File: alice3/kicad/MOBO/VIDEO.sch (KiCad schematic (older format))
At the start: 15 parts, among them SW1 RESET, U1 Propeller_P8X32A-D40, U2 VGA_daughter_board, U3 24LC256, U4 Propeller_Plug, U5 LM2937-3.3, Y1 5 MHz

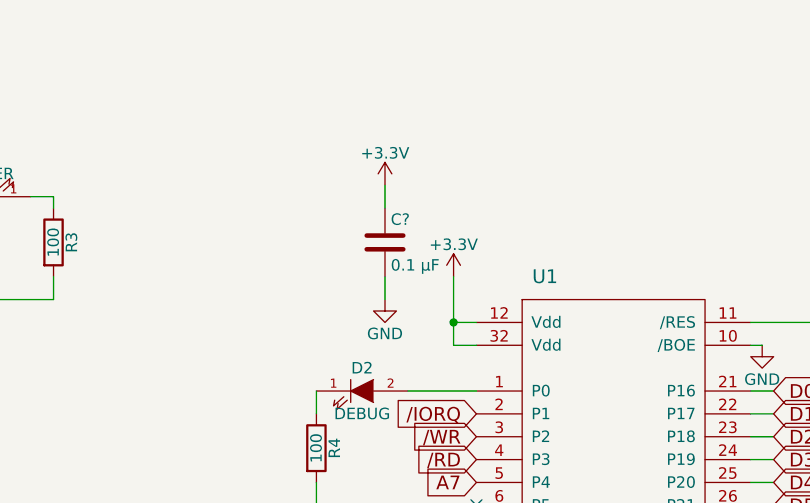
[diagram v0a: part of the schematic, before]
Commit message: Add SRAM and EEPROM.
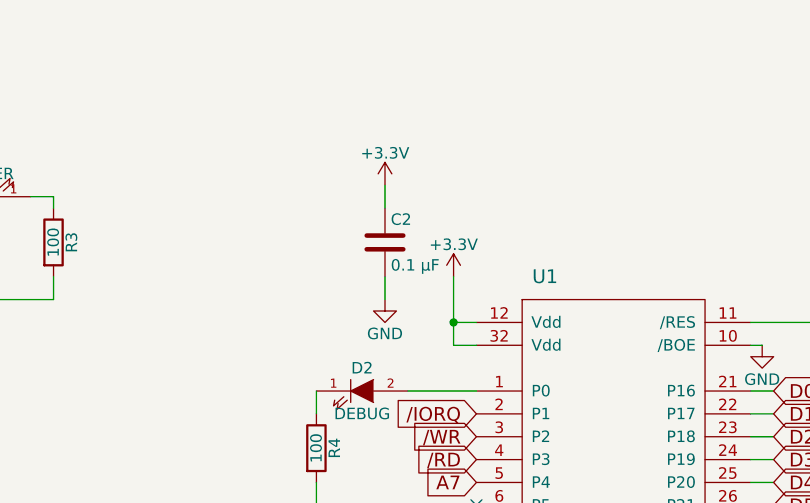
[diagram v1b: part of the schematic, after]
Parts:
- gave numbers to parts that had none: 1
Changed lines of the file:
@@
 LIBS:vga_daughter_board
 LIBS:Zilog
+LIBS:km681000blp-7
+LIBS:28f512
 LIBS:MOBO-cache
 EELAYER 25 0
@@
 $EndComp
 $Comp
-L GND #PWR01
+L GND #PWR12
 U 1 1 566E4A0D
 P 6100 4700
-F 0 "#PWR01" H 6100 4450 50  0001 C CNN
+F 0 "#PWR12" H 6100 4450 50  0001 C CNN
 F 1 "GND" H 6100 4550 50  0000 C CNN
 F 2 "" H 6100 4700 50  0000 C CNN
@@
 $EndComp
 $Comp
-L +3.3V #PWR02
+L +3.3V #PWR11
 U 1 1 566E4A37
 P 6100 2100
-F 0 "#PWR02" H 6100 1950 50  0001 C CNN
+F 0 "#PWR11" H 6100 1950 50  0001 C CNN
 F 1 "+3.3V" H 6100 2240 50  0000 C CNN
 F 2 "" H 6100 2100 50  0000 C CNN
@@
 $EndComp
 $Comp
-L +3.3V #PWR03
+L +3.3V #PWR14
 U 1 1 566E4B67
 P 7900 1700
-F 0 "#PWR03" H 7900 1550 50  0001 C CNN
+F 0 "#PWR14" H 7900 1550 50  0001 C CNN
 F 1 "+3.3V" H 7900 1840 50  0000 C CNN
 F 2 "" H 7900 1700 50  0000 C CNN
@@
 $EndComp
 $Comp
-L GND #PWR04
+L GND #PWR17
 U 1 1 566E4C07
 P 8650 2400
-F 0 "#PWR04" H 8650 2150 50  0001 C CNN
+F 0 "#PWR17" H 8650 2150 50  0001 C CNN
 F 1 "GND" H 8650 2250 50  0000 C CNN
 F 2 "" H 8650 2400 50  0000 C CNN
@@
 $EndComp
 $Comp
-L PWR_FLAG #FLG05
+L PWR_FLAG #FLG1
 U 1 1 566E4C94
 P 1000 1200
-F 0 "#FLG05" H 1000 1295 50  0001 C CNN
+F 0 "#FLG1" H 1000 1295 50  0001 C CNN
 F 1 "PWR_FLAG" H 1000 1380 50  0000 C CNN
 F 2 "" H 1000 1200 50  0000 C CNN
@@
 $EndComp
 $Comp
-L PWR_FLAG #FLG06
+L PWR_FLAG #FLG2
 U 1 1 566E4CCE
 P 1500 1200
-F 0 "#FLG06" H 1500 1295 50  0001 C CNN
+F 0 "#FLG2" H 1500 1295 50  0001 C CNN
 F 1 "PWR_FLAG" H 1500 1380 50  0000 C CNN
 F 2 "" H 1500 1200 50  0000 C CNN
@@
 $EndComp
 $Comp
-L GND #PWR07
+L GND #PWR2
 U 1 1 566E4D40
 P 1500 1500
-F 0 "#PWR07" H 1500 1250 50  0001 C CNN
+F 0 "#PWR2" H 1500 1250 50  0001 C CNN
 F 1 "GND" H 1500 1350 50  0000 C CNN
 F 2 "" H 1500 1500 50  0000 C CNN
@@
 $EndComp
 $Comp
-L GND #PWR08
+L GND #PWR16
 U 1 1 5681F164
 P 8350 4400
-F 0 "#PWR08" H 8350 4150 50  0001 C CNN
+F 0 "#PWR16" H 8350 4150 50  0001 C CNN
 F 1 "GND" H 8350 4250 50  0000 C CNN
 F 2 "" H 8350 4400 50  0000 C CNN
@@
 $EndComp
 $Comp
-L +3.3V #PWR09
+L +3.3V #PWR18
 U 1 1 5681F2C2
 P 9450 3850
-F 0 "#PWR09" H 9450 3700 50  0001 C CNN
+F 0 "#PWR18" H 9450 3700 50  0001 C CNN
 F 1 "+3.3V" H 9450 3990 50  0000 C CNN
 F 2 "" H 9450 3850 50  0000 C CNN
@@
 $EndComp
 $Comp
-L GND #PWR010
+L GND #PWR19
 U 1 1 5681F2E8
 P 9700 4150
-F 0 "#PWR010" H 9700 3900 50  0001 C CNN
+F 0 "#PWR19" H 9700 3900 50  0001 C CNN
 F 1 "GND" H 9700 4000 50  0000 C CNN
 F 2 "" H 9700 4150 50  0000 C CNN
@@
 $EndComp
 $Comp
-L +3.3V #PWR011
+L +3.3V #PWR15
 U 1 1 5681F435
 P 8100 3600
-F 0 "#PWR011" H 8100 3450 50  0001 C CNN
+F 0 "#PWR15" H 8100 3450 50  0001 C CNN
 F 1 "+3.3V" H 8100 3740 50  0000 C CNN
 F 2 "" H 8100 3600 50  0000 C CNN
@@
 $EndComp
 $Comp
-L GND #PWR012
+L GND #PWR4
 U 1 1 5681F91B
 P 2950 2350
-F 0 "#PWR012" H 2950 2100 50  0001 C CNN
+F 0 "#PWR4" H 2950 2100 50  0001 C CNN
 F 1 "GND" H 2950 2200 50  0000 C CNN
 F 2 "" H 2950 2350 50  0000 C CNN
@@
 $EndComp
 $Comp
-L +5V #PWR013
+L +5V #PWR3
 U 1 1 5681FA03
 P 2350 1650
-F 0 "#PWR013" H 2350 1500 50  0001 C CNN
+F 0 "#PWR3" H 2350 1500 50  0001 C CNN
 F 1 "+5V" H 2350 1790 50  0000 C CNN
 F 2 "" H 2350 1650 50  0000 C CNN
@@
 $EndComp
 $Comp
-L +3.3V #PWR014
+L +3.3V #PWR5
 U 1 1 5681FA32
 P 3550 1650
-F 0 "#PWR014" H 3550 1500 50  0001 C CNN
+F 0 "#PWR5" H 3550 1500 50  0001 C CNN
 F 1 "+3.3V" H 3550 1790 50  0000 C CNN
 F 2 "" H 3550 1650 50  0000 C CNN
@@
 $EndComp
 $Comp
-L +5V #PWR015
+L +5V #PWR1
 U 1 1 5681FAF3
 P 1000 1500
-F 0 "#PWR015" H 1000 1350 50  0001 C CNN
+F 0 "#PWR1" H 1000 1350 50  0001 C CNN
 F 1 "+5V" H 1000 1640 50  0000 C CNN
 F 2 "" H 1000 1500 50  0000 C CNN
@@
 $EndComp
 $Comp
-L GND #PWR016
+L GND #PWR6
 U 1 1 56821F3F
 P 5500 3100
-F 0 "#PWR016" H 5500 2850 50  0001 C CNN
+F 0 "#PWR6" H 5500 2850 50  0001 C CNN
 F 1 "GND" H 5500 2950 50  0000 C CNN
 F 2 "" H 5500 3100 50  0000 C CNN
@@
 NoConn ~ 7400 3800
 $Comp
-L GND #PWR021
+L GND #PWR13
 U 1 1 56826035
 P 7450 2400
-F 0 "#PWR021" H 7450 2150 50  0001 C CNN
+F 0 "#PWR13" H 7450 2150 50  0001 C CNN
 F 1 "GND" H 7450 2250 50  0000 C CNN
 F 2 "" H 7450 2400 50  0000 C CNN
@@
 	8300 2500 7850 2500
 $Comp
-L GND #PWR?
+L GND #PWR7
 U 1 1 568DCD28
 P 5600 4800
-F 0 "#PWR?" H 5600 4550 50  0001 C CNN
+F 0 "#PWR7" H 5600 4550 50  0001 C CNN
 F 1 "GND" H 5600 4650 50  0000 C CNN
 F 2 "" H 5600 4800 50  0000 C CNN
@@
 	5500 4800 5600 4800
 $Comp
-L +5V #PWR?
+L +5V #PWR10
 U 1 1 568DCDF3
 P 5900 4850
-F 0 "#PWR?" H 5900 4700 50  0001 C CNN
+F 0 "#PWR10" H 5900 4700 50  0001 C CNN
 F 1 "+5V" H 5900 4990 50  0000 C CNN
 F 2 "" H 5900 4850 50  0000 C CNN
@@
 /RD
 $Comp
-L C C?
+L C C2
 U 1 1 568DD525
 P 5800 1950
-F 0 "C?" H 5825 2050 50  0000 L CNN
+F 0 "C2" H 5825 2050 50  0000 L CNN
 F 1 "0.1 µF" H 5825 1850 50  0000 L CNN
 F 2 "" H 5838 1800 50  0000 C CNN
@@
 $EndComp
 $Comp
-L GND #PWR?
+L GND #PWR9
 U 1 1 568DD571
 P 5800 2200
-F 0 "#PWR?" H 5800 1950 50  0001 C CNN
+F 0 "#PWR9" H 5800 1950 50  0001 C CNN
 F 1 "GND" H 5800 2050 50  0000 C CNN
 F 2 "" H 5800 2200 50  0000 C CNN
@@
 $EndComp
 $Comp
-L +3.3V #PWR?
+L +3.3V #PWR8
 U 1 1 568DD5A9
 P 5800 1700
-F 0 "#PWR?" H 5800 1550 50  0001 C CNN
+F 0 "#PWR8" H 5800 1550 50  0001 C CNN
 F 1 "+3.3V" H 5800 1840 50  0000 C CNN
 F 2 "" H 5800 1700 50  0000 C CNN

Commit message: first draft completed integration
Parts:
- renumbered R3 to R1, R4 to R2, R1 to R3, R2 to R4, U5 to U1, U1 to U3, U3 to U4, U4 to U5
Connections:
- net CLK: now reaches U3.6 (P5)
- no-connect marks 9 -> 8
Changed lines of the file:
@@
 $EndDescr
 $Comp
-L Propeller_P8X32A-D40 U1
+L Propeller_P8X32A-D40 U3
 U 1 1 566E498F
 P 6800 3400
-F 0 "U1" H 6500 4700 60  0000 C CNN
+F 0 "U3" H 6500 4700 60  0000 C CNN
 F 1 "Propeller_P8X32A-D40" H 6800 2100 60  0000 C CNN
 F 2 "Housings_DIP:DIP-40_W25.4mm" H 6800 3200 60  0001 C CNN
@@
 $EndComp
 $Comp
-L GND #PWR12
+L GND #PWR01
 U 1 1 566E4A0D
 P 6100 4700
-F 0 "#PWR12" H 6100 4450 50  0001 C CNN
+F 0 "#PWR01" H 6100 4450 50  0001 C CNN
 F 1 "GND" H 6100 4550 50  0000 C CNN
 F 2 "" H 6100 4700 50  0000 C CNN
@@
 $EndComp
 $Comp
-L +3.3V #PWR11
+L +3.3V #PWR02
 U 1 1 566E4A37
 P 6100 2100
-F 0 "#PWR11" H 6100 1950 50  0001 C CNN
+F 0 "#PWR02" H 6100 1950 50  0001 C CNN
 F 1 "+3.3V" H 6100 2240 50  0000 C CNN
 F 2 "" H 6100 2100 50  0000 C CNN
@@
 $EndComp
 $Comp
-L +3.3V #PWR14
+L +3.3V #PWR03
 U 1 1 566E4B67
 P 7900 1700
-F 0 "#PWR14" H 7900 1550 50  0001 C CNN
+F 0 "#PWR03" H 7900 1550 50  0001 C CNN
 F 1 "+3.3V" H 7900 1840 50  0000 C CNN
 F 2 "" H 7900 1700 50  0000 C CNN
@@
 $EndComp
 $Comp
-L R R1
+L R R3
 U 1 1 566E4B83
 P 7900 1950
-F 0 "R1" V 7980 1950 50  0000 C CNN
+F 0 "R3" V 7980 1950 50  0000 C CNN
 F 1 "10K" V 7900 1950 50  0000 C CNN
 F 2 "Resistors_ThroughHole:Resistor_Horizontal_RM10mm" V 7830 1950 50  0001 C CNN
@@
 $EndComp
 $Comp
-L GND #PWR17
+L GND #PWR04
 U 1 1 566E4C07
 P 8650 2400
-F 0 "#PWR17" H 8650 2150 50  0001 C CNN
+F 0 "#PWR04" H 8650 2150 50  0001 C CNN
 F 1 "GND" H 8650 2250 50  0000 C CNN
 F 2 "" H 8650 2400 50  0000 C CNN
@@
 $EndComp
 $Comp
-L PWR_FLAG #FLG1
-U 1 1 566E4C94
-P 1000 1200
-F 0 "#FLG1" H 1000 1295 50  0001 C CNN
-F 1 "PWR_FLAG" H 1000 1380 50  0000 C CNN
-F 2 "" H 1000 1200 50  0000 C CNN
-F 3 "" H 1000 1200 50  0000 C CNN
-	1    1000 1200
-	1    0    0    -1
-$EndComp
-$Comp
-L PWR_FLAG #FLG2
-U 1 1 566E4CCE
-P 1500 1200
-F 0 "#FLG2" H 1500 1295 50  0001 C CNN
-F 1 "PWR_FLAG" H 1500 1380 50  0000 C CNN
-F 2 "" H 1500 1200 50  0000 C CNN
-F 3 "" H 1500 1200 50  0000 C CNN
-	1    1500 1200
-	1    0    0    -1
-$EndComp
-$Comp
-L GND #PWR2
-U 1 1 566E4D40
-P 1500 1500
-F 0 "#PWR2" H 1500 1250 50  0001 C CNN
-F 1 "GND" H 1500 1350 50  0000 C CNN
-F 2 "" H 1500 1500 50  0000 C CNN
-F 3 "" H 1500 1500 50  0000 C CNN
-	1    1500 1500
-	1    0    0    -1
-$EndComp
-$Comp
 L VGA_daughter_board U2
 U 1 1 5681E1A9
 P 5000 4150
-AR Path="/5681E1A9" Ref="U2"  Part="1"
-AR Path="/568DB7FD/5681E1A9" Ref="U2"  Part="1"
 F 0 "U2" H 4750 4950 60  0000 C CNN
 F 1 "VGA_daughter_board" H 5000 3300 60  0000 C CNN
@@
 $EndComp
 $Comp
-L 24LC256 U3
+L 24LC256 U4
 U 1 1 5681F117
 P 8900 4150
-F 0 "U3" H 8650 4450 60  0000 C CNN
+F 0 "U4" H 8650 4450 60  0000 C CNN
 F 1 "24LC256" H 8800 3850 60  0000 C CNN
 F 2 "Housings_DIP:DIP-8_W7.62mm" H 8900 4050 60  0001 C CNN
@@
 $EndComp
 $Comp
-L GND #PWR16
+L GND #PWR05
 U 1 1 5681F164
 P 8350 4400
-F 0 "#PWR16" H 8350 4150 50  0001 C CNN
+F 0 "#PWR05" H 8350 4150 50  0001 C CNN
 F 1 "GND" H 8350 4250 50  0000 C CNN
 F 2 "" H 8350 4400 50  0000 C CNN
@@
 $EndComp
 $Comp
-L +3.3V #PWR18
+L +3.3V #PWR06
 U 1 1 5681F2C2
 P 9450 3850
-F 0 "#PWR18" H 9450 3700 50  0001 C CNN
+F 0 "#PWR06" H 9450 3700 50  0001 C CNN
 F 1 "+3.3V" H 9450 3990 50  0000 C CNN
 F 2 "" H 9450 3850 50  0000 C CNN
@@
 $EndComp
 $Comp
-L GND #PWR19
+L GND #PWR07
 U 1 1 5681F2E8
 P 9700 4150
-F 0 "#PWR19" H 9700 3900 50  0001 C CNN
+F 0 "#PWR07" H 9700 3900 50  0001 C CNN
 F 1 "GND" H 9700 4000 50  0000 C CNN
 F 2 "" H 9700 4150 50  0000 C CNN
@@
 $EndComp
 $Comp
-L +3.3V #PWR15
+L +3.3V #PWR08
 U 1 1 5681F435
 P 8100 3600
-F 0 "#PWR15" H 8100 3450 50  0001 C CNN
+F 0 "#PWR08" H 8100 3450 50  0001 C CNN
 F 1 "+3.3V" H 8100 3740 50  0000 C CNN
 F 2 "" H 8100 3600 50  0000 C CNN
@@
 $EndComp
 $Comp
-L R R2
+L R R4
 U 1 1 5681F454
 P 8100 3800
-F 0 "R2" V 8180 3800 50  0000 C CNN
+F 0 "R4" V 8180 3800 50  0000 C CNN
 F 1 "10k" V 8100 3800 50  0000 C CNN
 F 2 "Resistors_ThroughHole:Resistor_Horizontal_RM10mm" V 8030 3800 50  0001 C CNN
@@
 $EndComp
 $Comp
-L Propeller_Plug U4
+L Propeller_Plug U5
 U 1 1 5681F4AC
 P 9600 2850
-F 0 "U4" H 9500 3150 60  0000 C CNN
+F 0 "U5" H 9500 3150 60  0000 C CNN
 F 1 "Propeller_Plug" H 9650 2500 60  0000 C CNN
 F 2 "Pin_Headers:Pin_Header_Straight_1x04" H 9600 2850 60  0001 C CNN
@@
 $EndComp
 $Comp
-L LM2937-3.3 U5
+L LM2937-3.3 U1
 U 1 1 5681F8BE
 P 2950 1800
-F 0 "U5" H 2700 2000 60  0000 C CNN
+F 0 "U1" H 2700 2000 60  0000 C CNN
 F 1 "LM2937-3.3" H 3150 2000 60  0000 C CNN
 F 2 "Power_Integrations:TO-220" H 2950 1800 60  0001 C CNN
@@
 $EndComp
 $Comp
-L GND #PWR4
+L GND #PWR09
 U 1 1 5681F91B
 P 2950 2350
-F 0 "#PWR4" H 2950 2100 50  0001 C CNN
+F 0 "#PWR09" H 2950 2100 50  0001 C CNN
 F 1 "GND" H 2950 2200 50  0000 C CNN
 F 2 "" H 2950 2350 50  0000 C CNN
@@
 $EndComp
 $Comp
-L +5V #PWR3
+L +5V #PWR010
 U 1 1 5681FA03
 P 2350 1650
-F 0 "#PWR3" H 2350 1500 50  0001 C CNN
+F 0 "#PWR010" H 2350 1500 50  0001 C CNN
 F 1 "+5V" H 2350 1790 50  0000 C CNN
 F 2 "" H 2350 1650 50  0000 C CNN
@@
 $EndComp
 $Comp
-L +3.3V #PWR5
+L +3.3V #PWR011
 U 1 1 5681FA32
 P 3550 1650
-F 0 "#PWR5" H 3550 1500 50  0001 C CNN
+F 0 "#PWR011" H 3550 1500 50  0001 C CNN
 F 1 "+3.3V" H 3550 1790 50  0000 C CNN
 F 2 "" H 3550 1650 50  0000 C CNN
@@
 	1    3550 1650
 	1    0    0    -1
-$EndComp
-$Comp
-L +5V #PWR1
-U 1 1 5681FAF3
-P 1000 1500
-F 0 "#PWR1" H 1000 1350 50  0001 C CNN
-F 1 "+5V" H 1000 1640 50  0000 C CNN
-F 2 "" H 1000 1500 50  0000 C CNN
-F 3 "" H 1000 1500 50  0000 C CNN
-	1    1000 1500
-	-1   0    0    1
 $EndComp
 $Comp
@@
 $EndComp
 $Comp
-L R R3
+L R R1
 U 1 1 5681FD9C
 P 4350 1950
-F 0 "R3" V 4430 1950 50  0000 C CNN
+F 0 "R1" V 4430 1950 50  0000 C CNN
 F 1 "100" V 4350 1950 50  0000 C CNN
 F 2 "Resistors_ThroughHole:Resistor_Horizontal_RM10mm" V 4280 1950 50  0001 C CNN
@@
 $EndComp
 $Comp
-L R R4
+L R R2
 U 1 1 56821F00
 P 5500 2850
-F 0 "R4" V 5580 2850 50  0000 C CNN
+F 0 "R2" V 5580 2850 50  0000 C CNN
 F 1 "100" V 5500 2850 50  0000 C CNN
 F 2 "Resistors_ThroughHole:Resistor_Horizontal_RM10mm" V 5430 2850 50  0001 C CNN
@@
 $EndComp
 $Comp
-L GND #PWR6
+L GND #PWR012
 U 1 1 56821F3F
 P 5500 3100
-F 0 "#PWR6" H 5500 2850 50  0001 C CNN
+F 0 "#PWR012" H 5500 2850 50  0001 C CNN
 F 1 "GND" H 5500 2950 50  0000 C CNN
 F 2 "" H 5500 3100 50  0000 C CNN
@@
 NoConn ~ 7400 3800
 $Comp
-L GND #PWR13
+L GND #PWR013
 U 1 1 56826035
 P 7450 2400
-F 0 "#PWR13" H 7450 2150 50  0001 C CNN
+F 0 "#PWR013" H 7450 2150 50  0001 C CNN
 F 1 "GND" H 7450 2250 50  0000 C CNN
 F 2 "" H 7450 2400 50  0000 C CNN
@@
 Connection ~ 7900 2300
 Wire Wire Line
-	1500 1200 1500 1500
-Wire Wire Line
-	1000 1200 1000 1500
-Wire Wire Line
 	5500 3500 6200 3500
 Wire Wire Line
@@
 	8300 2500 7850 2500
 $Comp
-L GND #PWR7
+L GND #PWR014
 U 1 1 568DCD28
 P 5600 4800
-F 0 "#PWR7" H 5600 4550 50  0001 C CNN
+F 0 "#PWR014" H 5600 4550 50  0001 C CNN
 F 1 "GND" H 5600 4650 50  0000 C CNN
 F 2 "" H 5600 4800 50  0000 C CNN
@@
 	5500 4800 5600 4800
 $Comp
-L +5V #PWR10
+L +5V #PWR015
 U 1 1 568DCDF3
 P 5900 4850
-F 0 "#PWR10" H 5900 4700 50  0001 C CNN
+F 0 "#PWR015" H 5900 4700 50  0001 C CNN
 F 1 "+5V" H 5900 4990 50  0000 C CNN
 F 2 "" H 5900 4850 50  0000 C CNN
@@
 Text GLabel 6200 3000 0    60   Input ~ 0
 A7
-NoConn ~ 6200 3100
 NoConn ~ 6200 3200
 Text GLabel 6200 2900 0    60   Input ~ 0
@@
 $EndComp
 $Comp
-L GND #PWR9
+L GND #PWR016
 U 1 1 568DD571
 P 5800 2200
-F 0 "#PWR9" H 5800 1950 50  0001 C CNN
+F 0 "#PWR016" H 5800 1950 50  0001 C CNN
 F 1 "GND" H 5800 2050 50  0000 C CNN
 F 2 "" H 5800 2200 50  0000 C CNN
@@
 $EndComp
 $Comp
-L +3.3V #PWR8
+L +3.3V #PWR017
 U 1 1 568DD5A9
 P 5800 1700
-F 0 "#PWR8" H 5800 1550 50  0001 C CNN
+F 0 "#PWR017" H 5800 1550 50  0001 C CNN
 F 1 "+3.3V" H 5800 1840 50  0000 C CNN
 F 2 "" H 5800 1700 50  0000 C CNN
@@
 Wire Wire Line
 	5800 2100 5800 2200
+Text GLabel 6200 3100 0    60   Output ~ 0
+CLK
 $EndSCHEMATC
